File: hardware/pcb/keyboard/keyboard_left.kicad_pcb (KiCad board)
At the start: 2 copper layers, 133.8 x 110.4 mm, 118 parts, among them J1 SM04B-SRSS-TB, J2 TRRS PJ320D, J3 HRO_TYPE-C-31-M-12, J4 FH34SRJ-10S-0.5SH, Q1 AO3407, SW1 EC_SW, SW10 EC_SW, SW11 EC_SW, SW12 EC_SW, SW13 EC_SW, SW14 EC_SW, SW15 EC_SW, SW16 EC_SW, SW17 EC_SW, SW18 EC_SW, SW19 EC_SW, SW2 EC_SW, SW20 EC_SW, SW21 EC_SW, SW22 EC_SW, SW23 EC_SW, SW24 EC_SW, SW25 EC_SW, SW26 EC_SW, SW27 EC_SW, SW28 EC_SW, SW29 SW_Push, SW3 EC_SW, SW4 EC_SW, SW5 EC_SW, SW6 EC_SW, SW7 EC_SW, SW8 EC_SW, SW9 EC_SW, U1 74HC4051, U2 OPA350UA, U3 nRF52840_holyiot_18010, U4 XC6220B331MR-G, U5 DT1446-04S, U6 DT1446-04S, U8 TP4054

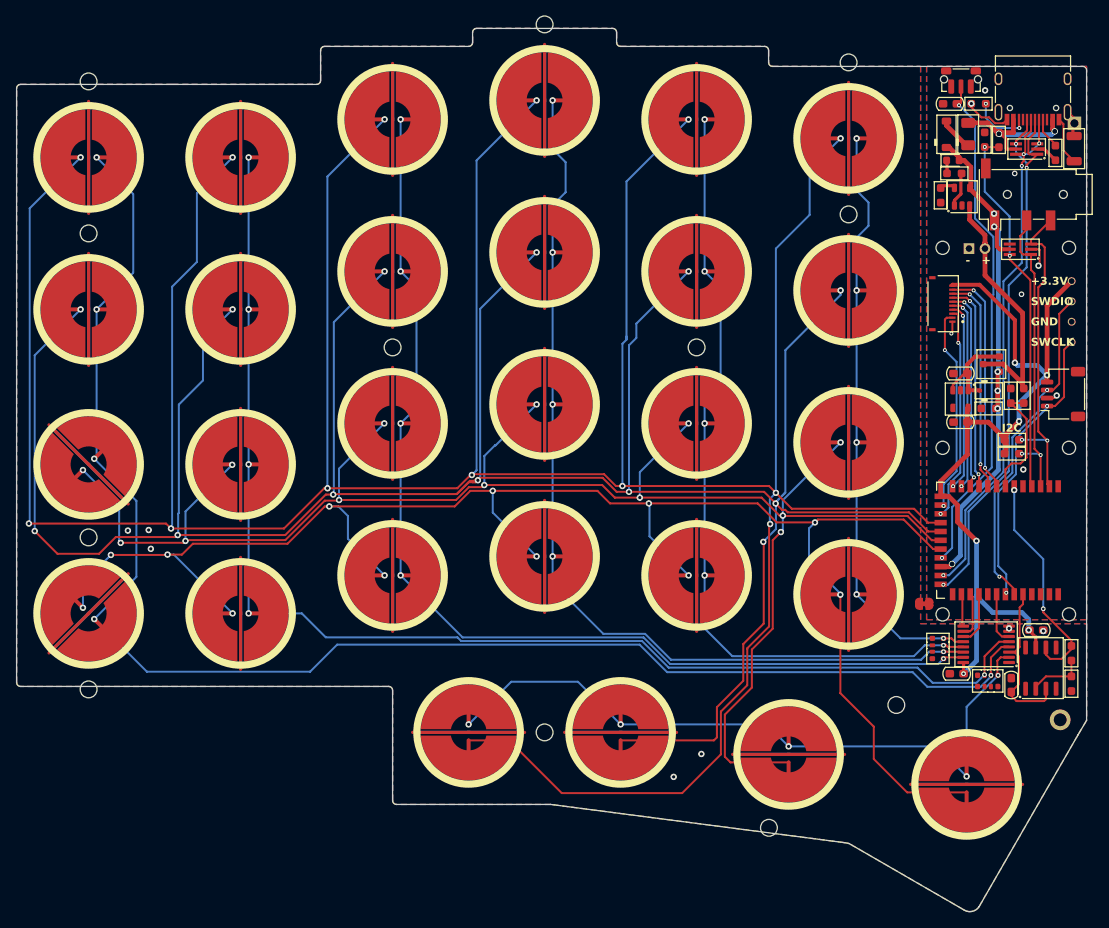
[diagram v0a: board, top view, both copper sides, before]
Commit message: Init STM32G0 PCB
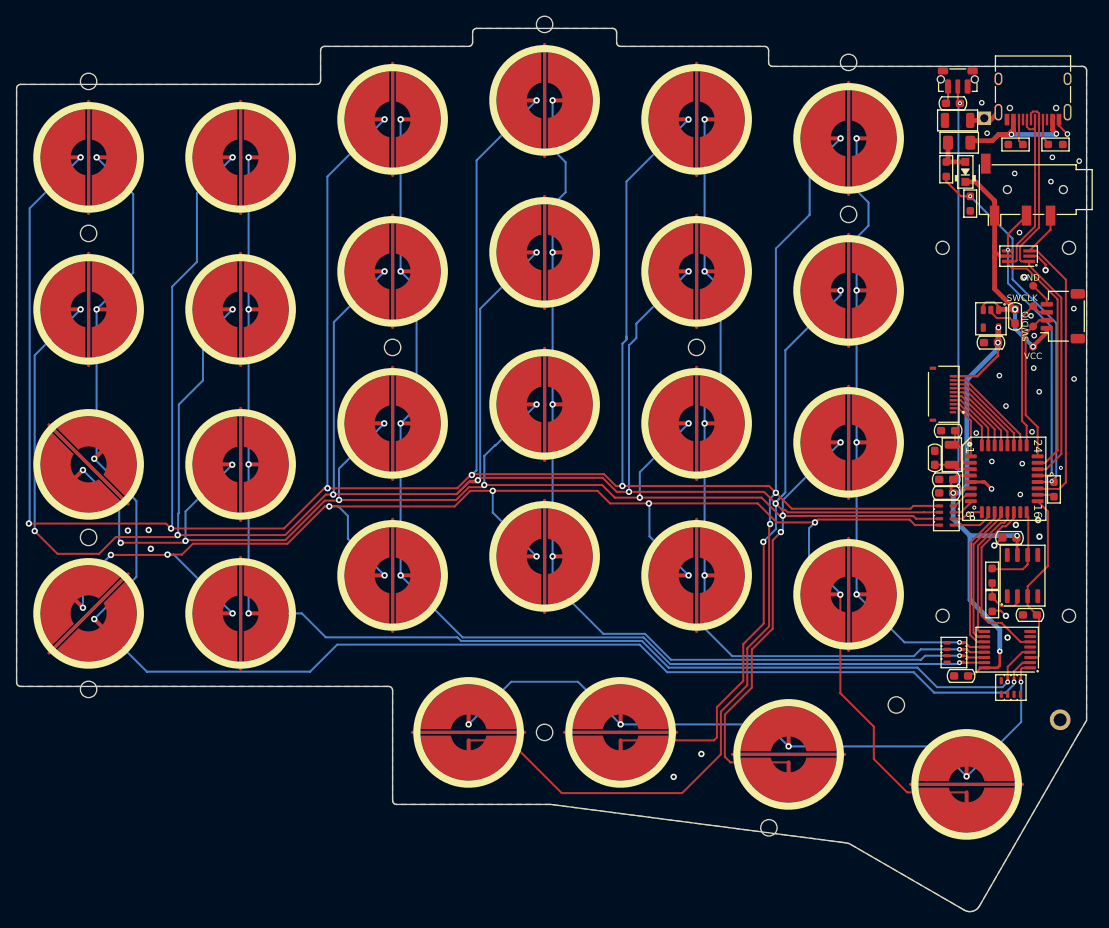
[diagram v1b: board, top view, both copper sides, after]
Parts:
- removed the D1 at (187.8, 67.9)
- removed D2: LED 0603 RED, LED_SMD:LED_0603_1608Metric
- removed the H13 at (197.8, 75.0)
- removed the H16 at (182.0, 75.0)
- removed J5: ~, ec_parts:PinHeader_1x04_P2.54mm_top_only
- removed J6: ~, ec_parts:PinHeader_1x02_P2.00mm_Vertical
- removed JP1: ~, ec_parts:P1.3mm_Bridged_RoundedPad1.0x1.5mm
- removed Q1: AO3407, PCM_Package_TO_SOT_SMD_AKL:SOT-23
- removed R11: 820K, PCM_Resistor_SMD_AKL:R_0603_1608Metric_Pad0.98x0.95mm
- removed R12: 2M, PCM_Resistor_SMD_AKL:R_0603_1608Metric_Pad0.98x0.95mm
- removed R13: 1k, PCM_Resistor_SMD_AKL:R_0603_1608Metric_Pad0.98x0.95mm
- removed R15: RPROG, PCM_Resistor_SMD_AKL:R_0603_1608Metric_Pad0.98x0.95mm
- removed the R3 at (187.8, 70.1)
- removed the R7 at (190.7, 74.0)
- removed R8: 3.3k, PCM_Resistor_SMD_AKL:R_0603_1608Metric_Pad0.98x0.95mm
- removed U6: DT1446-04S, PCM_Package_TO_SOT_SMD_AKL:SOT-363_SC-70-6_Handsoldering
- removed U8: TP4054, PCM_Package_TO_SOT_SMD_AKL:SOT-23-5
- added C1: 0.1uF, PCM_Capacitor_SMD_AKL:C_0603_1608Metric_Pad1.05x0.95mm, F.Cu at (183.3, 31.9)
- added C6: 5.6p, PCM_Capacitor_SMD_AKL:C_0603_1608Metric_Pad1.05x0.95mm, F.Cu at (182.7, 72.9)
- added C7: 5.6p, PCM_Capacitor_SMD_AKL:C_0603_1608Metric_Pad1.05x0.95mm, F.Cu at (181.0, 76.3)
- added C8: 1uF, PCM_Capacitor_SMD_AKL:C_0603_1608Metric_Pad1.05x0.95mm, F.Cu at (188.0, 61.9)
- added R1: 1k, PCM_Resistor_SMD_AKL:R_0603_1608Metric_Pad0.98x0.95mm, F.Cu at (195.9, 80.2)
- added RN3: 100 R_Array_Convex_4x1206, PCM_Resistor_SMD_AKL:R_Array_Concave_4x0603, F.Cu at (182.5, 83.5)
- added TP1: ~, ec_parts:PinHeader_1x04_P2.54mm_test_pad, F.Cu at (193.3, 62.4)
- added Y1: NX3215SA, PCM_Crystal_AKL:Crystal_SMD_3215-2Pin_3.2x1.5mm, F.Cu at (183.2, 75.9)
- C10: renamed from C16; footprint PCM_Capacitor_SMD_AKL:C_0603_1608Metric_Pad1.08x0.95mm -> PCM_Capacitor_SMD_AKL:C_0603_1608Metric_Pad1.05x0.95mm
- C2: footprint PCM_Capacitor_SMD_AKL:C_0603_1608Metric_Pad1.08x0.95mm -> PCM_Capacitor_SMD_AKL:C_0603_1608Metric_Pad1.05x0.95mm
- C3: renamed from C6; footprint PCM_Capacitor_SMD_AKL:C_0603_1608Metric_Pad1.08x0.95mm -> PCM_Capacitor_SMD_AKL:C_0603_1608Metric_Pad1.05x0.95mm
- C4: value 1uF -> 0.1uF; footprint PCM_Capacitor_SMD_AKL:C_0603_1608Metric_Pad1.08x0.95mm -> PCM_Capacitor_SMD_AKL:C_0603_1608Metric_Pad1.05x0.95mm
- C5: value 1uF -> 4.7u; footprint PCM_Capacitor_SMD_AKL:C_0603_1608Metric_Pad1.08x0.95mm -> PCM_Capacitor_SMD_AKL:C_0603_1608Metric_Pad1.05x0.95mm
- C9: renamed from C3; footprint PCM_Capacitor_SMD_AKL:C_0603_1608Metric_Pad1.08x0.95mm -> PCM_Capacitor_SMD_AKL:C_0603_1608Metric_Pad1.05x0.95mm
- D1: renamed from D3; footprint PCM_Diode_SMD_AKL:D_SOD-123 -> PCM_Diode_SMD_AKL:D_SOD-323_HandSoldering
- H1, H10, H11, H12, H2, H3, H4, H5, H6, H7, H8, H9: footprint MountingHole:MountingHole_2.1mm -> ec_parts:MountingHole_2.05mm
- J2: value TRRS PJ320D -> PJ320D
- RN1, RN2: value 4x0604 1k resistor array -> 1k R_Array_Concave_4x0603; footprint PCM_Resistor_SMD_AKL:R_Array_Convex_4x0612 -> PCM_Resistor_SMD_AKL:R_Array_Concave_4x0603
- SW1, SW10, SW11, SW12, SW13, SW14, SW15, SW16, SW17, SW18, SW19, SW2, SW20, SW21, SW22, SW23, SW24, SW25, SW26, SW27, SW28, SW3, SW4, SW5, SW6, SW7, SW8, SW9: value EC_SW -> ~
- SW29: value SW_Push -> PTS845
- U3: value nRF52840_holyiot_18010 -> DT1446-04S; footprint PCM_marbastlib-various:nRF52840_holyiot_18010_HS_simple -> PCM_Package_TO_SOT_SMD_AKL:SOT-363_SC-70-6_Handsoldering
- U5: value DT1446-04S -> STM32G0B1KETx; footprint PCM_Package_TO_SOT_SMD_AKL:SOT-363_SC-70-6_Handsoldering -> PCM_Package_QFP_AKL:LQFP-32_7x7mm_P0.8mm
- moved C5 46.9 mm to (182.5, 78.9)
- moved U3 35.5 mm to (191.5, 51.0), turned to 180 degrees
- moved U5 28.8 mm to (189.7, 78.9), turned to 0 degrees
- moved L1 15.0 mm to (183.9, 34.1), turned to 0 degrees
- moved R6 14.0 mm to (188.2, 94.5)
- moved R7 13.9 mm to (188.2, 91.0)
- moved C2 12.0 mm to (190.4, 86.3), turned to 0 degrees
- moved U2 11.8 mm to (192.0, 91.0)
- moved J4 11.3 mm to (182.1, 68.3)
- moved H17 11.3 mm to (187.2, 33.8), turned to -90 degrees
- moved U4 10.7 mm to (188.0, 58.9)
- moved C9 9.88 mm to (191.1, 58.6), turned to -90 degrees
- moved J1 9.73 mm to (197.0, 58.6)
- moved C10 9.06 mm to (192.9, 95.9), turned to 180 degrees
- moved C4 9.03 mm to (182.5, 80.6)
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- renumbered H19 to H13, H18 to H16, R4 to R2, R2 to R3, R5 to R4, R6 to R5, R9 to R6, R10 to R7
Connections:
- C10 pad 2: GNDA -> GND
- C2 pad 1: GNDA -> GND
- C3 pad 1: GNDA -> GND
- C5 pad 1: RESET -> +3V3
- C9 pad 1: VSYS -> +5V
- D1 pad 2: Net-(D3-A) -> Net-(D1-A)
- F1 pad 1: Net-(D3-A) -> Net-(D1-A)
- H0 pad 1: GNDA -> GND
- H17 pad 1: USB_SHILED_1 -> GNDPWR
- J1 pad 1: SWDCLK -> +5V
- J1 pad 2: GND -> SWDIO
- J1 pad 3: SWDIO -> SWCLK
- J1 pad 4: +3V3 -> GND
- J2 pad R1: SCL -> USART_RX
- J2 pad R2: SDA -> USART_TX
- J3 pad S1: USB_SHILED_1 -> unconnected-(J3-SHIELD-PadS1)
- J3 pad S2: USB_SHILED_2 -> GNDPWR
- L1 pad 2: USB_SHILED_1 -> GNDPWR
- R4 pad 1: VBUS -> Net-(D1-A)
- R6 pad 2: GNDA -> GND
- RN1 pad 5: GNDA -> GND
- RN1 pad 6: GNDA -> GND
- RN1 pad 7: GNDA -> GND
- RN1 pad 8: GNDA -> GND
- RN2 pad 1: A6 -> A4
- RN2 pad 2: A7 -> A6
- RN2 pad 3: A5 -> A7
- RN2 pad 5: GNDA -> GND
- RN2 pad 6: GNDA -> GND
- RN2 pad 7: GNDA -> GND
- RN2 pad 8: GNDA -> GND
- SW1 pad 1: A7 -> A6
- SW1 pad 3: GNDA -> GND
- SW10 pad 3: GNDA -> GND
- SW11 pad 3: GNDA -> GND
- SW12 pad 3: GNDA -> GND
- SW13 pad 3: GNDA -> GND
- SW14 pad 3: GNDA -> GND
- SW15 pad 3: GNDA -> GND
- SW16 pad 3: GNDA -> GND
- SW17 pad 3: GNDA -> GND
- SW18 pad 3: GNDA -> GND
- SW19 pad 3: GNDA -> GND
- SW2 pad 1: A7 -> A6
- SW2 pad 3: GNDA -> GND
- SW20 pad 1: A6 -> A4
- SW20 pad 3: GNDA -> GND
- SW21 pad 1: A6 -> A4
- SW21 pad 3: GNDA -> GND
- SW22 pad 1: A6 -> A4
- SW22 pad 3: GNDA -> GND
- SW23 pad 1: A5 -> A7
- SW23 pad 3: GNDA -> GND
- SW24 pad 3: GNDA -> GND
- SW25 pad 3: GNDA -> GND
- SW26 pad 3: GNDA -> GND
- SW27 pad 3: GNDA -> GND
- SW28 pad 1: A6 -> A4
- SW28 pad 3: GNDA -> GND
- SW29 pad 2: RESET -> /NRST
- SW3 pad 1: A7 -> A6
- SW3 pad 3: GNDA -> GND
- SW4 pad 1: A7 -> A6
- SW4 pad 3: GNDA -> GND
- SW5 pad 1: A5 -> A7
- SW5 pad 3: GNDA -> GND
- SW6 pad 1: A5 -> A7
- SW6 pad 3: GNDA -> GND
- SW7 pad 1: A5 -> A7
- SW7 pad 3: GNDA -> GND
- SW8 pad 3: GNDA -> GND
- SW9 pad 3: GNDA -> GND
- U1 pad 7: GNDA -> GND
- U1 pad 8: GNDA -> GND
- U2 pad 4: GNDA -> GND
- U3 pad 1: GND -> D-
- U3 pad 2: SDA -> GND
- U3 pad 3: SCL -> USART_TX
- U3 pad 4: VBUS_DEC -> USART_RX
- U3 pad 5: unconnected-(U3-P1.15-LF-Pad5) -> +5V
- U3 pad 6: ADC -> D+
- U4 pad 1: VSYS -> +5V
- U4 pad 3: VSYS -> +5V
- U5 pad 1: SCL -> ACCS_8
- U5 pad 2: GND -> /OSC32_IN
- U5 pad 3: SDA -> /OSC32_OUT
- U5 pad 4: unconnected-(U5-IO3-Pad4) -> +3V3
- U5 pad 5: +5V -> GND
- U5 pad 6: VBUS_DEC -> /NRST
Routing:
- net A5: track 159.1 -> 0.00 mm, vias 5 -> 0
- net A6: track 86.5 -> 192.5 mm
- net A4: track 0.00 -> 87.2 mm, vias 0 -> 5
- net RESET: track 63.1 -> 0.00 mm, vias 2 -> 0
- net /NRST: track 0.00 -> 51.4 mm, vias 0 -> 2
- net USART_TX: track 0.00 -> 40.7 mm
- net SDA: track 39.8 -> 0.00 mm, vias 2 -> 0
- net SCL: track 37.6 -> 0.00 mm, vias 2 -> 0
- net USART_RX: track 0.00 -> 37.5 mm, vias 0 -> 2
- net SWDCLK: track 36.1 -> 0.00 mm, vias 2 -> 0
- net +5V: track 69.1 -> 35.9 mm, vias 6 -> 2
- net VBAT: track 31.5 -> 0.00 mm
- net +3V3: track 102.6 -> 74.1 mm, vias 6 -> 5
- net A7: track 190.1 -> 161.8 mm
- net SWDIO: track 41.6 -> 19.3 mm, vias 2 -> 0
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- removed copper zone on B.Cu, net GNDA
- removed copper zone on F.Cu, net GNDA
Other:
- board text added: "VCC"
- board text removed: "+"
- board text removed: "+3.3V"
- board text removed: "-"
- board text removed: "I2C"

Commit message: Fix capacitor, resistor values
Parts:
- C6, C7: value 5.6p -> 22p
- R4: value 10k -> < 800
- R5: value 5.6k -> 1k
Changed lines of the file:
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@@
   (title_block
     (title "Corne EEC")
-    (date "2023-06-22")
+    (date "2023-07-18")
     (rev "1.0")
     (comment 1 "Copyright © 2023")
@@
         (effects (font (size 1 1) (thickness 0.15)))
     )
-    (fp_text value "5.6p" (at 0 1.43 90) (layer "F.Fab") hide
+    (fp_text value "22p" (at 0 1.43 90) (layer "F.Fab") hide
         (effects (font (size 1 1) (thickness 0.15)))
     )
@@
         (effects (font (size 1 1) (thickness 0.15)))
     )
-    (fp_text value "5.6p" (at 0 1.43) (layer "F.Fab") hide
+    (fp_text value "22p" (at 0 1.43) (layer "F.Fab") hide
         (effects (font (size 1 1) (thickness 0.15)))
     )
@@
         (effects (font (size 1 1) (thickness 0.15)))
     )
-    (fp_text value "10k" (at 0 1.43 90) (layer "F.Fab") hide
+    (fp_text value "< 800" (at 0 1.43 90) (layer "F.Fab") hide
         (effects (font (size 1 1) (thickness 0.15)))
     )
@@
         (effects (font (size 1 1) (thickness 0.15)))
     )
-    (fp_text value "5.6k" (at 0 1.43 90) (layer "F.Fab") hide
+    (fp_text value "1k" (at 0 1.43 90) (layer "F.Fab") hide
         (effects (font (size 1 1) (thickness 0.15)))
     )
